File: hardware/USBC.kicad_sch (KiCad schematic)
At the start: 16 parts, among them J601 2305018-2, U601 CP2102N-A02-GQFN20, U602 CDSOT236-0504C

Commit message: reannotate
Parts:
- renumbered C601 to C501, C602 to C502, D601 to D501, D602 to D502, D603 to D503, J601 to J501, R601 to R501, R602 to R502, R603 to R503, R604 to R504, R605 to R505, R606 to R506, R607 to R507, R608 to R508, U601 to U501, U602 to U502

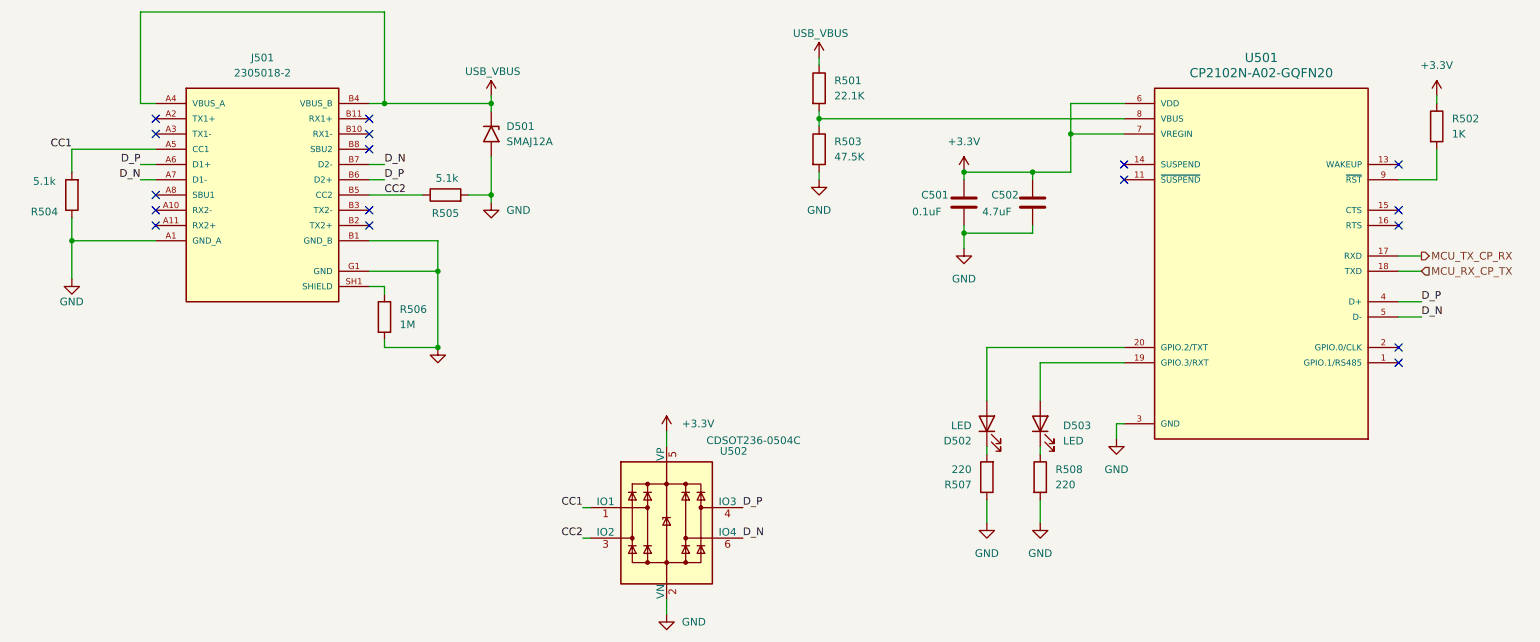
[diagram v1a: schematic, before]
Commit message: added QON pushbutton
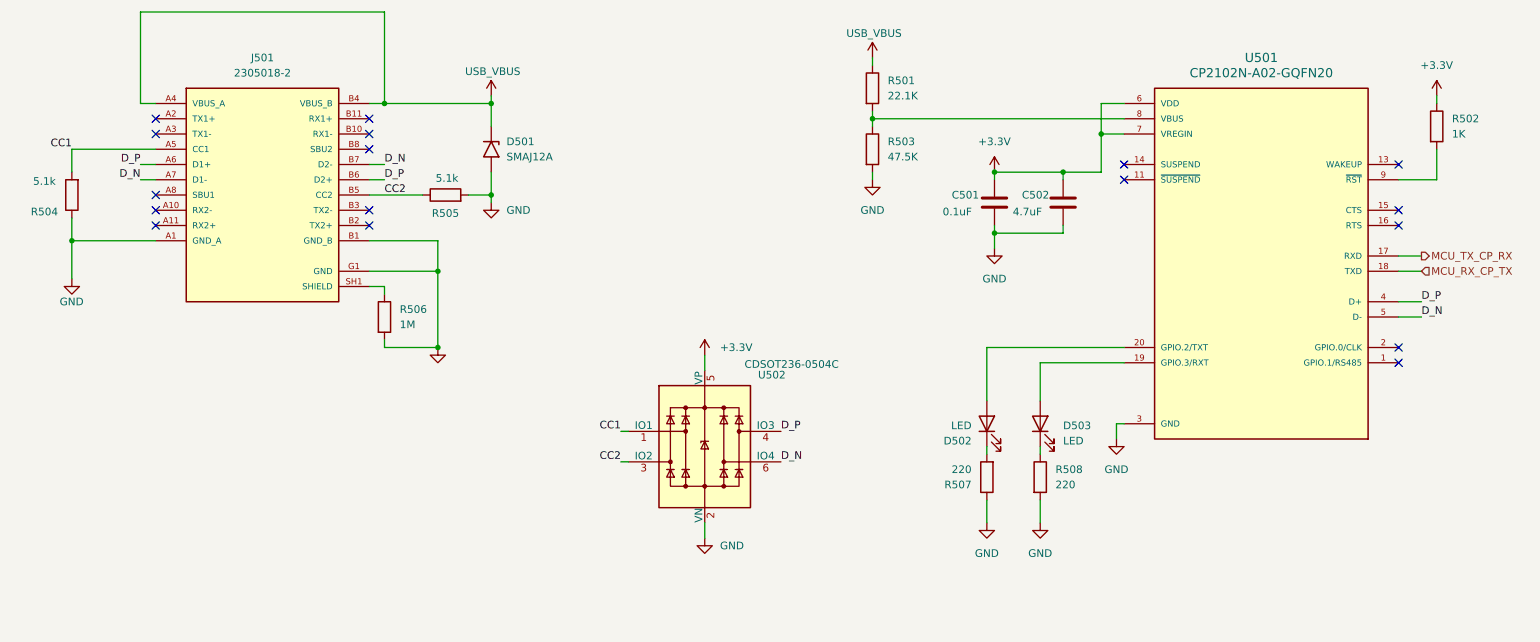
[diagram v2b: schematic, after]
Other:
- moved on the sheet: C501, C502, D501, R501, R503, U502

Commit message: PCB layout update
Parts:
- C501, C502: footprint Capacitor_SMD:C_0805_2012Metric -> Capacitor_SMD:C_0603_1608Metric
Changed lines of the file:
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@@
 			)
 		)
-		(property "Footprint" "Capacitor_SMD:C_0805_2012Metric"
+		(property "Footprint" "Capacitor_SMD:C_0603_1608Metric"
 			(at 199.0852 88.9 0)
 			(effects
@@
 			)
 		)
-		(property "Footprint" "Capacitor_SMD:C_0805_2012Metric"
+		(property "Footprint" "Capacitor_SMD:C_0603_1608Metric"
 			(at 187.6552 88.9 0)
 			(effects
@@
 					(size 1.27 1.27)
 				)
-				(hide yes)
-			)
-		)
+			)
+		)

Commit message: Added Mounting Holes
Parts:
- renumbered C502 to C?, C501 to C?, D501 to D?, D503 to D?, D502 to D?, J501 to J?, R508 to R?, R502 to R?, R504 to R?, R501 to R?, R505 to R?, R507 to R?, R503 to R?, R506 to R?, U501 to U?, U502 to U?

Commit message: 3dmodels update
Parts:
- gave numbers to parts that had none: 16
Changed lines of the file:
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@@
 		(on_board yes)
 		(dnp no)
-		(property "Reference" "C?"
+		(property "Reference" "C502"
 			(at 191.262 83.82 0)
 			(effects
@@
 		(dnp no)
 		(fields_autoplaced yes)
-		(property "Reference" "#PWR?"
+		(property "Reference" "#PWR0511"
 			(at 207.01 130.81 0)
 			(effects
@@
 		(dnp no)
 		(fields_autoplaced yes)
-		(property "Reference" "R?"
+		(property "Reference" "R508"
 			(at 196.85 129.5399 0)
 			(effects
@@
 		(dnp no)
 		(fields_autoplaced yes)
-		(property "Reference" "D?"
+		(property "Reference" "D501"
 			(at 105.41 74.9299 90)
 			(effects
@@
 		(dnp no)
 		(fields_autoplaced yes)
-		(property "Reference" "#PWR?"
+		(property "Reference" "#PWR0504"
 			(at 186.69 83.82 0)
 			(effects
@@
 		(dnp no)
 		(fields_autoplaced yes)
-		(property "Reference" "R?"
+		(property "Reference" "R502"
 			(at 262.89 71.1199 0)
 			(effects
@@
 		(dnp no)
 		(fields_autoplaced yes)
-		(property "Reference" "D?"
+		(property "Reference" "D503"
 			(at 198.12 122.2374 90)
 			(effects
@@
 		(on_board yes)
 		(dnp no)
-		(property "Reference" "#PWR?"
+		(property "Reference" "#PWR0505"
 			(at 166.37 87.63 0)
 			(effects
@@
 		(on_board yes)
 		(dnp no)
-		(property "Reference" "#PWR?"
+		(property "Reference" "#PWR0502"
 			(at 102.87 71.12 0)
 			(effects
@@
 		(on_board yes)
 		(dnp no)
-		(property "Reference" "R?"
+		(property "Reference" "R504"
 			(at 28.448 86.614 0)
 			(effects
@@
 		(dnp no)
 		(fields_autoplaced yes)
-		(property "Reference" "J?"
+		(property "Reference" "J501"
 			(at 64.77 60.96 0)
 			(effects
@@
 		(dnp no)
 		(fields_autoplaced yes)
-		(property "Reference" "#PWR?"
+		(property "Reference" "#PWR0513"
 			(at 194.31 144.78 0)
 			(effects
@@
 		(dnp no)
 		(fields_autoplaced yes)
-		(property "Reference" "R?"
+		(property "Reference" "R501"
 			(at 168.91 64.7699 0)
 			(effects
@@
 		(on_board yes)
 		(dnp no)
-		(property "Reference" "C?"
+		(property "Reference" "C501"
 			(at 179.578 83.82 0)
 			(effects
@@
 		(dnp no)
 		(fields_autoplaced yes)
-		(property "Reference" "#PWR?"
+		(property "Reference" "#PWR0507"
 			(at 186.69 99.06 0)
 			(effects
@@
 		(dnp no)
 		(fields_autoplaced yes)
-		(property "Reference" "#PWR?"
+		(property "Reference" "#PWR0512"
 			(at 185.42 144.78 0)
 			(effects
@@
 		(on_board yes)
 		(dnp no)
-		(property "Reference" "D?"
+		(property "Reference" "D502"
 			(at 182.88 124.7776 90)
 			(effects
@@
 		(on_board yes)
 		(dnp no)
-		(property "Reference" "#PWR?"
+		(property "Reference" "#PWR0501"
 			(at 166.37 64.77 0)
 			(effects
@@
 		(dnp no)
 		(fields_autoplaced yes)
-		(property "Reference" "#PWR?"
+		(property "Reference" "#PWR0510"
 			(at 138.43 114.3 0)
 			(effects
@@
 		(on_board yes)
 		(dnp no)
-		(property "Reference" "R?"
+		(property "Reference" "R505"
 			(at 95.25 86.868 90)
 			(effects
@@
 		(on_board yes)
 		(dnp no)
-		(property "Reference" "R?"
+		(property "Reference" "R507"
 			(at 182.88 132.0801 0)
 			(effects
@@
 		(dnp no)
 		(fields_autoplaced yes)
-		(property "Reference" "U?"
+		(property "Reference" "U501"
 			(at 231.14 60.96 0)
 			(effects
@@
 		(on_board yes)
 		(dnp no)
-		(property "Reference" "#PWR?"
+		(property "Reference" "#PWR0506"
 			(at 102.87 91.44 0)
 			(effects
@@
 		(on_board yes)
 		(dnp no)
-		(property "Reference" "U?"
+		(property "Reference" "U502"
 			(at 149.606 113.792 0)
 			(effects
@@
 		(dnp no)
 		(fields_autoplaced yes)
-		(property "Reference" "#PWR?"
+		(property "Reference" "#PWR0503"
 			(at 260.35 71.12 0)
 			(effects
@@
 		(dnp no)
 		(fields_autoplaced yes)
-		(property "Reference" "R?"
+		(property "Reference" "R503"
 			(at 168.91 74.9299 0)
 			(effects
@@
 		(dnp no)
 		(fields_autoplaced yes)
-		(property "Reference" "#PWR?"
+		(property "Reference" "#PWR0509"
 			(at 93.98 115.57 0)
 			(effects
@@
 		(on_board yes)
 		(dnp no)
-		(property "Reference" "#PWR?"
+		(property "Reference" "#PWR0508"
 			(at 33.02 104.14 0)
 			(effects
@@
 		(dnp no)
 		(fields_autoplaced yes)
-		(property "Reference" "R?"
+		(property "Reference" "R506"
 			(at 87.63 102.8699 0)
 			(effects
@@
 		(dnp no)
 		(fields_autoplaced yes)
-		(property "Reference" "#PWR?"
+		(property "Reference" "#PWR0514"
 			(at 138.43 147.32 0)
 			(effects

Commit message: USB update
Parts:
- removed J501: 2305018-2, pyronet_footprints:TE_2305018-2, symbol pyronet_symbols:2305018-2
- added J501: USB4105-GF-A, pyronet_footprints:GCT_USB4105-GF-A, symbol pyronet_symbols:USB4105-GF-A
- R506: value 1M -> 0
- renumbered R505 to R504, R504 to R505
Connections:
- net CC1: now also J501.A5 (CC1)
- net CC2: now also J501.B5 (CC2)
- net D_N: now also J501.A7 (DN1), J501.B6 (DP2)
- net D_P: now also J501.A6 (DP1), J501.B7 (DN2)
- net GND: now also J501.A1_B12 (GND), J501.B1_A12 (GND__1)
- net USB_VBUS: now also J501.A4_B9 (VBUS), J501.B4_A9 (VBUS__1)
- net at R506.1: now also J501.SH1 (SHELL_GND), J501.SH2 (SHELL_GND__1), J501.SH3 (SHELL_GND__2), J501.SH4 (SHELL_GND__3)
- no-connect marks 17 -> 9
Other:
- moved on the sheet: D501, R504, R505, R506, U502

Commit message: PCB cleanup
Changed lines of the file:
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@@
 		)
 		(property "Footprint" "Capacitor_SMD:C_0603_1608Metric"
-			(at 187.6552 88.9 0)
+			(at 166.878 96.012 0)
 			(effects
 				(font
 					(size 1.27 1.27)
 				)
+				(hide yes)
 			)
 		)
